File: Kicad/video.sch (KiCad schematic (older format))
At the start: 1 part

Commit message: Completed Audio sheet.
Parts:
- gave numbers to parts that had none: 1
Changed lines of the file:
@@
 Sheet 2 9
 Title ""
-Date ""
+Date "2020-12-20"
 Rev ""
-Comp ""
-Comment1 ""
-Comment2 ""
+Comp "https://neotron-compute.github.io/"
+Comment1 "Licenced as CC BY-SA"
+Comment2 "Copyright (c) The Neotron Developers, 2020"
 Comment3 ""
 Comment4 ""
 $EndDescr
 $Comp
-L Connector:DB15_Female_HighDensity_MountingHoles J?
+L Connector:DB15_Female_HighDensity_MountingHoles J201
 U 1 1 5FDEDC06
 P 4450 3300
-F 0 "J?" V 4496 4029 50  0000 L CNN
+F 0 "J201" V 4496 4029 50  0000 L CNN
 F 1 "DB15_Female_HighDensity_MountingHoles" V 4025 2680 50  0000 L CNN
 F 2 "Connector_Dsub:DSUB-15-HD_Male_Horizontal_P2.29x1.98mm_EdgePinOffset3.03mm_Housed_MountingHolesOffset4.94mm" H 3500 3700 50  0001 C CNN

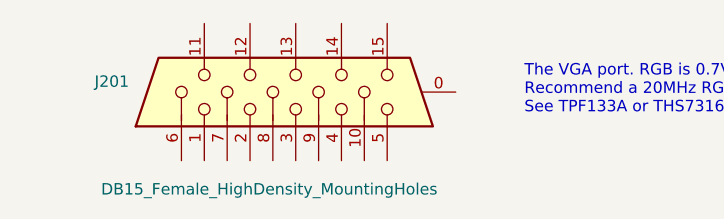
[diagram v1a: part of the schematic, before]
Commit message: Brought in RS232 circuit from Neotron 32.
Also updated 3D models.
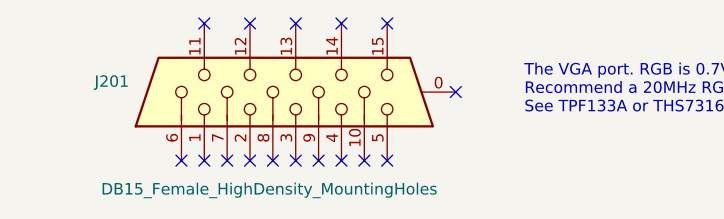
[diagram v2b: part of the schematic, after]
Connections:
- no-connect marks 0 -> 16
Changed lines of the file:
@@
 Text Notes 5450 3400 0    50   ~ 0
 The VGA port. RGB is 0.7V p-p into 75 ohms. HSync and VSync is TTL.\nRecommend a 20MHz RGB video buffer to avoid overloading GPIO pins.\nSee TPF133A or THS7316.
+NoConn ~ 3950 3600
+NoConn ~ 4050 3600
+NoConn ~ 4150 3600
+NoConn ~ 4250 3600
+NoConn ~ 4350 3600
+NoConn ~ 4450 3600
+NoConn ~ 4550 3600
+NoConn ~ 4650 3600
+NoConn ~ 4750 3600
+NoConn ~ 4850 3600
+NoConn ~ 5150 3300
+NoConn ~ 4850 3000
+NoConn ~ 4650 3000
+NoConn ~ 4450 3000
+NoConn ~ 4250 3000
+NoConn ~ 4050 3000
 $EndSCHEMATC

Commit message: Updating BOM with parts.
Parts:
- J201: DNP (none) -> 0
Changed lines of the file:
@@
 F 2 "Connector_Dsub:DSUB-15-HD_Male_Horizontal_P2.29x1.98mm_EdgePinOffset3.03mm_Housed_MountingHolesOffset4.94mm" H 3500 3700 50  0001 C CNN
 F 3 " ~" H 3500 3700 50  0001 C CNN
+F 4 "0" H 4450 3300 50  0001 C CNN "DNP"
 	1    4450 3300
 	0    -1   -1   0

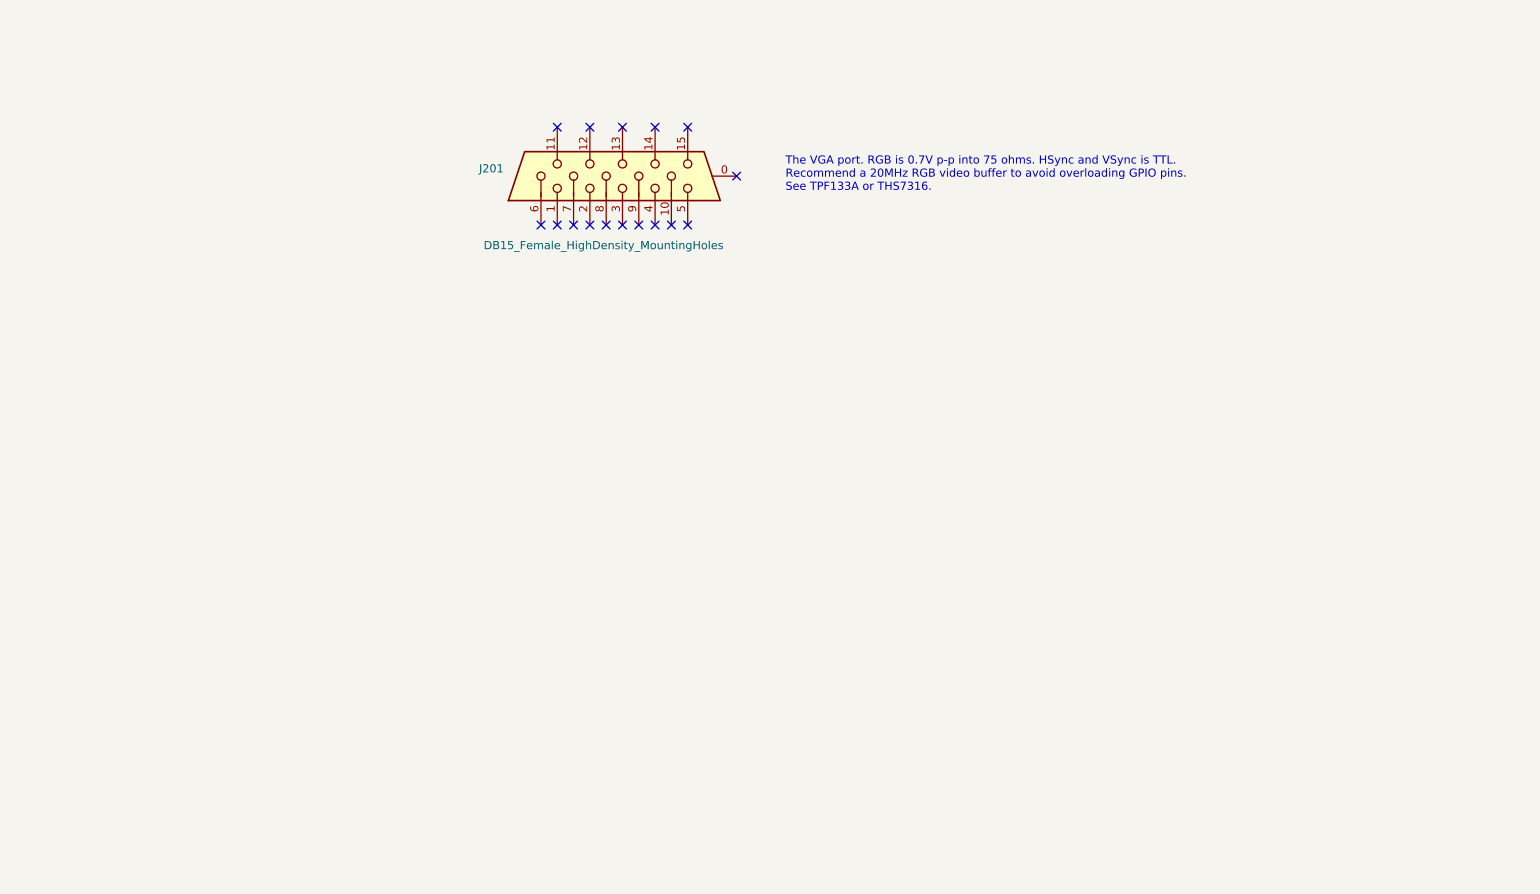
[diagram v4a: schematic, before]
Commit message: Working on VGA sheet and USB sheet.
Also added courtyard and silk to stacked USB connector.
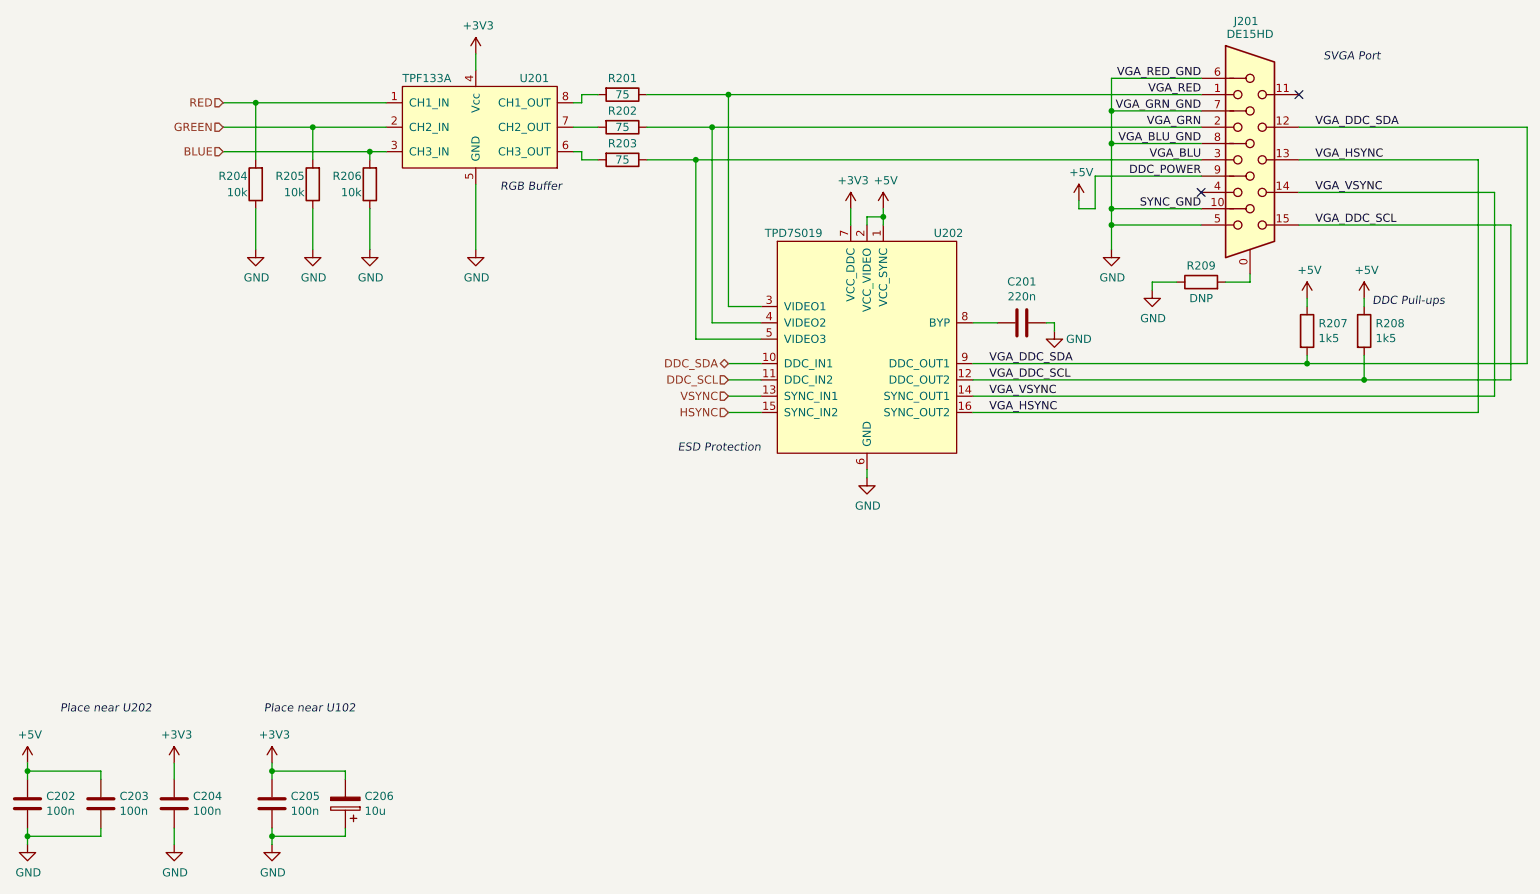
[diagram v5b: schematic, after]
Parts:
- added C201: 220n, Capacitor_SMD:C_0805_2012Metric_Pad1.15x1.40mm_HandSolder, symbol Device:C
- added C202, C203, C204, C205: 100n, Capacitor_SMD:C_0805_2012Metric_Pad1.15x1.40mm_HandSolder, symbol Device:C
- added C206: 10u, Capacitor_THT:CP_Radial_D6.3mm_P2.50mm, symbol Device:CP
- added R201, R202, R203: 75, Resistor_SMD:R_0805_2012Metric_Pad1.15x1.40mm_HandSolder, symbol Device:R
- added R204, R205, R206: 10k, Resistor_SMD:R_0805_2012Metric_Pad1.15x1.40mm_HandSolder, symbol Device:R
- added R207, R208: 1k5, Resistor_SMD:R_0805_2012Metric_Pad1.15x1.40mm_HandSolder, symbol Device:R
- added R209: DNP, Resistor_SMD:R_0805_2012Metric_Pad1.15x1.40mm_HandSolder, symbol Device:R
- added U201: TPF133A, Package_SO:SOIC-8_3.9x4.9mm_P1.27mm, symbol Neotron-Common-Hardware:TPF133A
- added U202: TPD7S019, Package_SO:SSOP-16_3.9x4.9mm_P0.635mm, symbol Neotron-Common-Hardware:TPD7S019
- J201: value DB15_Female_HighDensity_MountingHoles -> DE15HD; footprint Connector_Dsub:DSUB-15-HD_Male_Horizontal_P2.29x1.98mm_EdgePinOffset3.03mm_Housed_MountingHolesOffset4.94mm -> Connector_Dsub:DSUB-15-HD_Female_Horizontal_P2.29x1.98mm_EdgePinOffset3.03mm_Housed_MountingHolesOffset4.94mm
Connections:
- net at J201.0: now also R209.2
- net VGA_RED: now reaches J201.1
- net VGA_RED: now also R201.1, U202.3 (VIDEO1)
- net GND: now reaches J201.10
- net GND: now also J201.5, J201.6, J201.7, J201.8, C201.1, C202.1, C203.1, C204.1, C205.1, C206.1, R204.1, R205.1, R206.1, R209.1, U201.5 (GND), U202.6 (GND)
- net VGA_DDC_SDA: now reaches J201.12
- net VGA_DDC_SDA: now also R207.2, U202.9 (DDC_OUT1)
- net VGA_HSYNC: now reaches J201.13
- net VGA_HSYNC: now also U202.16 (SYNC_OUT2)
- net VGA_VSYNC: now reaches J201.14
- net VGA_VSYNC: now also U202.14 (SYNC_OUT1)
- net VGA_DDC_SCL: now reaches J201.15
- net VGA_DDC_SCL: now also R208.2, U202.12 (DDC_OUT2)
- net VGA_GRN: now reaches J201.2
- net VGA_GRN: now also R202.1, U202.4 (VIDEO2)
- net VGA_BLU: now reaches J201.3
- net VGA_BLU: now also R203.1, U202.5 (VIDEO3)
- net +5V: now reaches J201.9
- net +5V: now also C202.2, C203.2, R207.1, R208.1, U202.1 (VCC_SYNC), U202.2 (VCC_VIDEO)
- new net: R201.2, U201.8 (CH1_OUT)
- new net: R202.2, U201.7 (CH2_OUT)
- new net: R203.2, U201.6 (CH3_OUT)
- new net: C201.2, U202.8 (BYP)
- new net +3V3: C204.2, C205.2, C206.2, U201.4 (Vcc), U202.7 (VCC_DDC)
- new net BLUE: R206.2, U201.3 (CH3_IN)
- new net DDC_SCL: U202.11 (DDC_IN2)
- new net DDC_SDA: U202.10 (DDC_IN1)
- new net GREEN: R205.2, U201.2 (CH2_IN)
- new net HSYNC: U202.15 (SYNC_IN2)
- new net RED: R204.2, U201.1 (CH1_IN)
- new net VSYNC: U202.13 (SYNC_IN1)
- no-connect marks 16 -> 2
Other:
- note added: "DDC Pull-ups"
- note added: "ESD Protection"
- note added: "Place near U102"
- note added: "Place near U202"
- note added: "RGB Buffer"
- note added: "SVGA Port"
- note removed: "The VGA port. RGB is 0.7V p-p into 75 ohms. HSync and VSync is TTL.\nRecommend a 20MHz RGB video buffer to avoid overloading GPIO pins.\nSee TPF133A or THS7316."
- moved on the sheet: J201
